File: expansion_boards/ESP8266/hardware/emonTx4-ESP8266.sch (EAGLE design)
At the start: 13 parts, among them IC1 2471

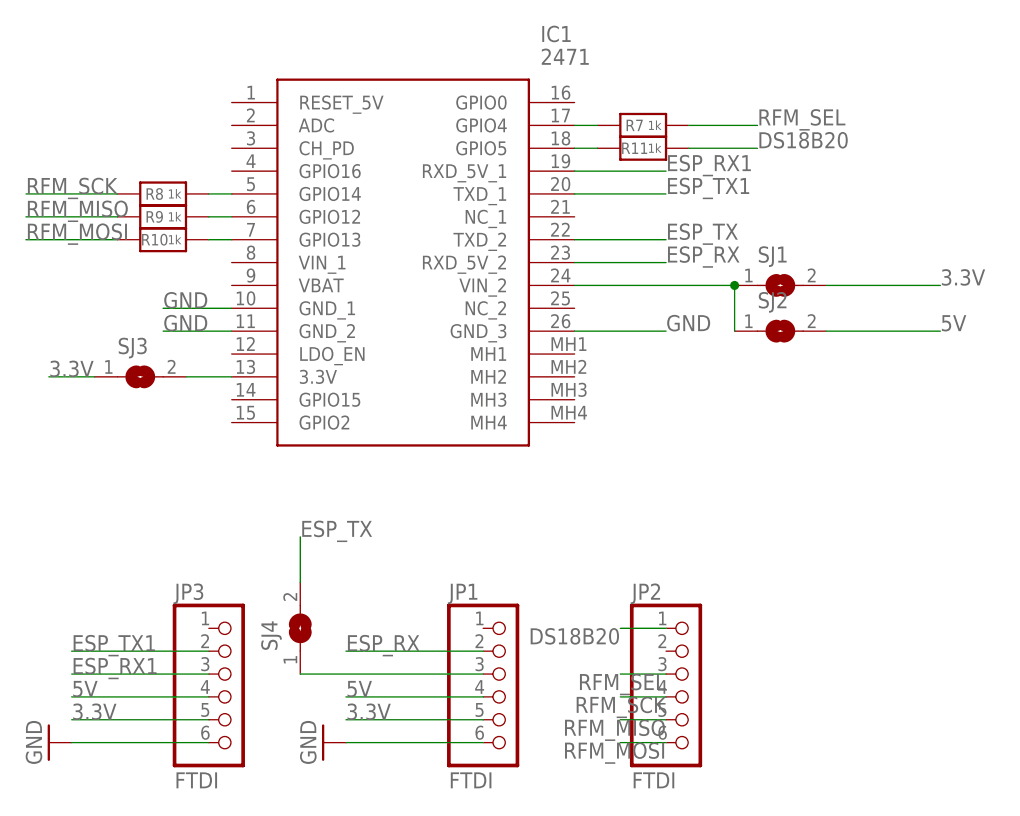
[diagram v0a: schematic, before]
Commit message: updated ESP8266 adapter board
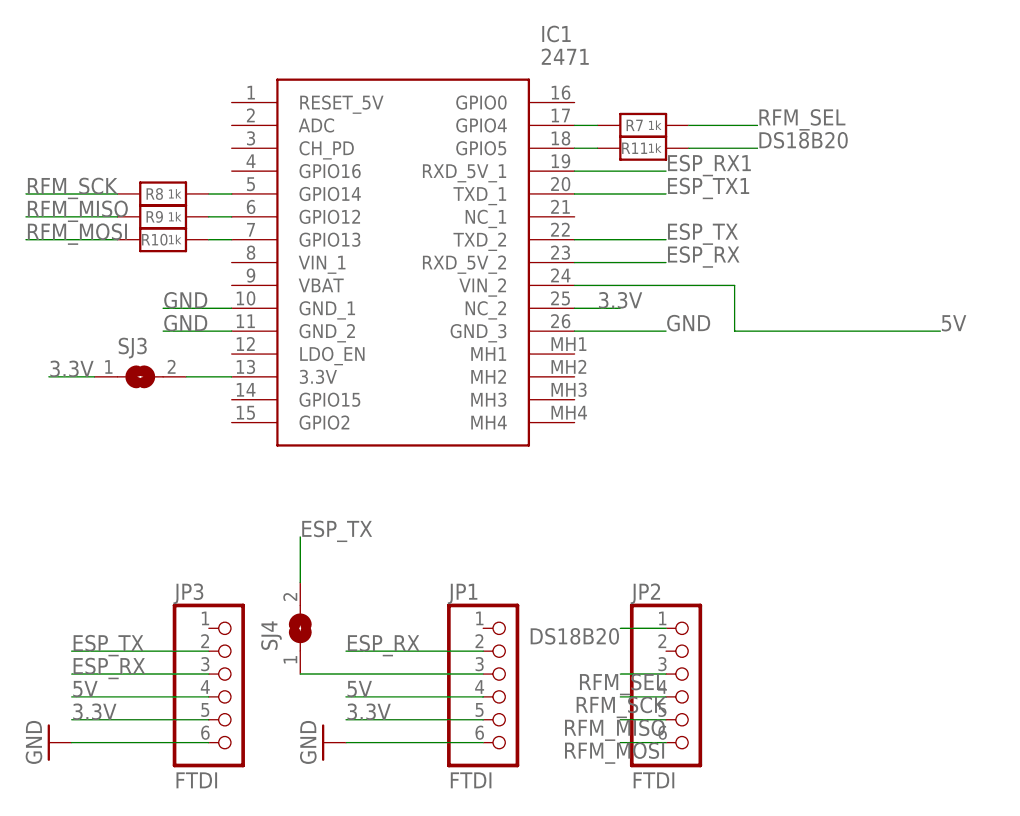
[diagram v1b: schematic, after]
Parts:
- removed SJ1, SJ2: (no value), jumper:SJ
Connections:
- removed net N$6: IC1.VIN_2, SJ1.1, SJ2.1
- net 3.3V: now also IC1.NC_2; no longer SJ1.2
- net 5V: now also IC1.VIN_2; no longer SJ2.2
- net ESP_RX: now also JP3.3
- net ESP_RX1: no longer JP3.3
- net ESP_TX: now also JP3.2
- net ESP_TX1: no longer JP3.2
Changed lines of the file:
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@@
 <part name="JP3" library="microbuilder" deviceset="HEADER-1X6" device="70MIL" value="FTDI"/>
 <part name="IC1" library="2471" deviceset="2471" device=""/>
-<part name="SJ1" library="jumper" library_urn="urn:adsk.eagle:library:252" deviceset="SJ" device="" package3d_urn="urn:adsk.eagle:package:15471/1"/>
-<part name="SJ2" library="jumper" library_urn="urn:adsk.eagle:library:252" deviceset="SJ" device="" package3d_urn="urn:adsk.eagle:package:15471/1"/>
 <part name="SJ3" library="jumper" library_urn="urn:adsk.eagle:library:252" deviceset="SJ" device="" package3d_urn="urn:adsk.eagle:package:15471/1"/>
 <part name="R7" library="microbuilder" deviceset="RESISTOR" device="_0603" value="1k"/>
@@
 <attribute name="VALUE" x="105.41" y="119.38" size="1.778" layer="96" align="center-left"/>
 </instance>
-<instance part="SJ1" gate="1" x="132.08" y="93.98" smashed="yes">
-<attribute name="NAME" x="129.54" y="96.52" size="1.778" layer="95"/>
-<attribute name="VALUE" x="129.54" y="90.17" size="1.778" layer="96"/>
-</instance>
-<instance part="SJ2" gate="1" x="132.08" y="88.9" smashed="yes">
-<attribute name="NAME" x="129.54" y="91.44" size="1.778" layer="95"/>
-<attribute name="VALUE" x="129.54" y="85.09" size="1.778" layer="96"/>
-</instance>
 <instance part="SJ3" gate="1" x="60.96" y="83.82" smashed="yes">
 <attribute name="NAME" x="58.42" y="86.36" size="1.778" layer="95"/>
@@
 </segment>
 <segment>
-<pinref part="SJ1" gate="1" pin="2"/>
-<wire x1="137.16" y1="93.98" x2="149.86" y2="93.98" width="0.1524" layer="91"/>
-<label x="149.86" y="93.98" size="1.778" layer="95"/>
-</segment>
-<segment>
 <pinref part="SJ3" gate="1" pin="1"/>
 <wire x1="55.88" y1="83.82" x2="50.8" y2="83.82" width="0.1524" layer="91"/>
 <label x="50.8" y="83.82" size="1.778" layer="95"/>
 </segment>
+<segment>
+<pinref part="IC1" gate="G$1" pin="NC_2"/>
+<wire x1="109.22" y1="91.44" x2="114.3" y2="91.44" width="0.1524" layer="91"/>
+<label x="111.76" y="91.44" size="1.778" layer="95"/>
+</segment>
 </net>
 <net name="DS18B20" class="0">
@@
 <pinref part="JP1" gate="A" pin="2"/>
 </segment>
+<segment>
+<pinref part="JP3" gate="A" pin="3"/>
+<wire x1="68.58" y1="50.8" x2="53.34" y2="50.8" width="0.1524" layer="91"/>
+<label x="53.34" y="50.8" size="1.778" layer="95"/>
+</segment>
 </net>
 <net name="ESP_TX" class="0">
@@
 <label x="78.74" y="66.04" size="1.778" layer="95"/>
 </segment>
-</net>
-<net name="N$6" class="0">
-<segment>
+<segment>
+<pinref part="JP3" gate="A" pin="2"/>
+<wire x1="68.58" y1="53.34" x2="53.34" y2="53.34" width="0.1524" layer="91"/>
+<label x="53.34" y="53.34" size="1.778" layer="95"/>
+</segment>
+</net>
+<net name="5V" class="0">
+<segment>
+<wire x1="127" y1="88.9" x2="149.86" y2="88.9" width="0.1524" layer="91"/>
+<label x="149.86" y="88.9" size="1.778" layer="95"/>
 <pinref part="IC1" gate="G$1" pin="VIN_2"/>
 <wire x1="109.22" y1="93.98" x2="127" y2="93.98" width="0.1524" layer="91"/>
-<pinref part="SJ1" gate="1" pin="1"/>
-<junction x="127" y="93.98"/>
-<pinref part="SJ2" gate="1" pin="1"/>
 <wire x1="127" y1="93.98" x2="127" y2="88.9" width="0.1524" layer="91"/>
-</segment>
-</net>
-<net name="5V" class="0">
-<segment>
-<pinref part="SJ2" gate="1" pin="2"/>
-<wire x1="137.16" y1="88.9" x2="149.86" y2="88.9" width="0.1524" layer="91"/>
-<label x="149.86" y="88.9" size="1.778" layer="95"/>
 </segment>
 <segment>
@@
 <label x="119.38" y="106.68" size="1.778" layer="95"/>
 </segment>
-<segment>
-<pinref part="JP3" gate="A" pin="3"/>
-<wire x1="68.58" y1="50.8" x2="53.34" y2="50.8" width="0.1524" layer="91"/>
-<label x="53.34" y="50.8" size="1.778" layer="95"/>
-</segment>
 </net>
 <net name="ESP_TX1" class="0">
@@
 <label x="119.38" y="104.14" size="1.778" layer="95"/>
 </segment>
-<segment>
-<pinref part="JP3" gate="A" pin="2"/>
-<wire x1="68.58" y1="53.34" x2="53.34" y2="53.34" width="0.1524" layer="91"/>
-<label x="53.34" y="53.34" size="1.778" layer="95"/>
-</segment>
-</net>
+</net>
